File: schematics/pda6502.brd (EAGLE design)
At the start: 100 x 80 mm, 35 parts, among them IC1 74HC00D, IC2 74HC138D, IC3 DS1813-SMD, J1 CON_HEADER_2X07-PTH, U1 W65C02S, U2 W65C22S, U3 28C256, U4 UM61256AK-12

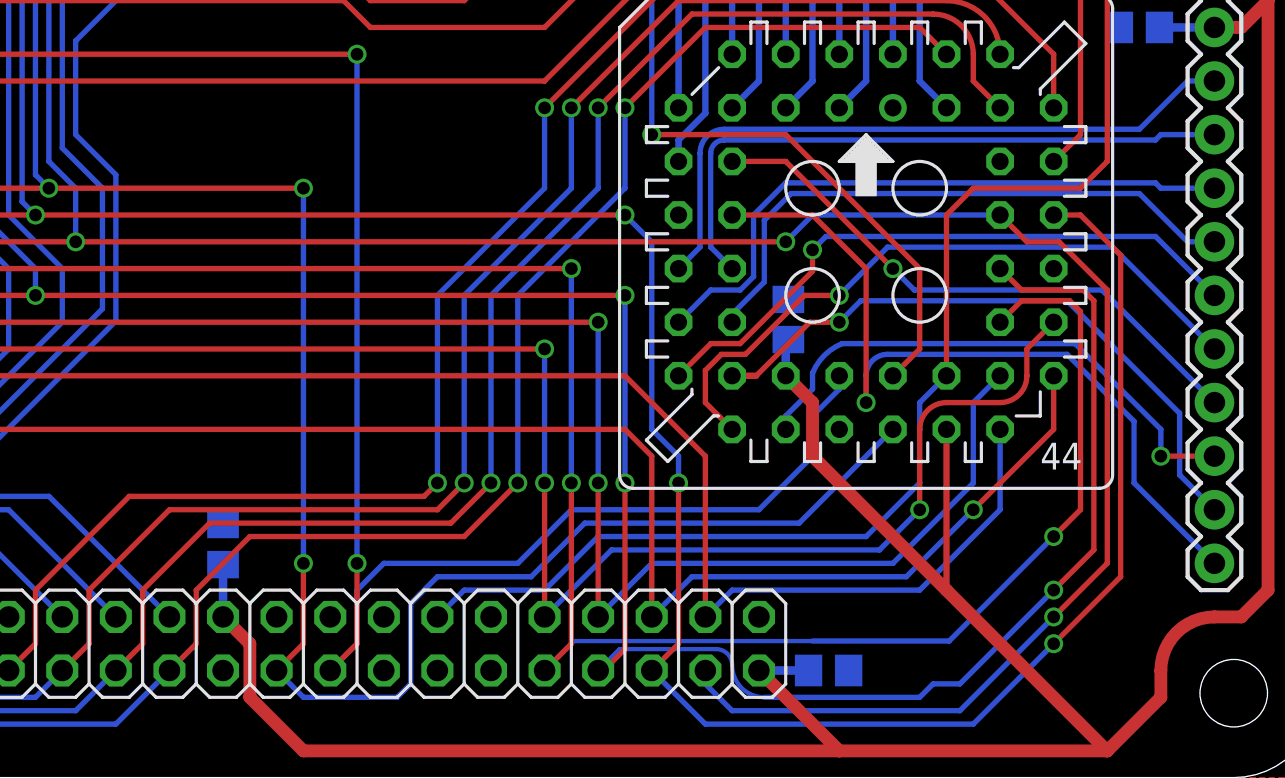
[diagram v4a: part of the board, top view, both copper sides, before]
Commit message: board: tweaks to maximize bottom GND plane; 4 airwires.
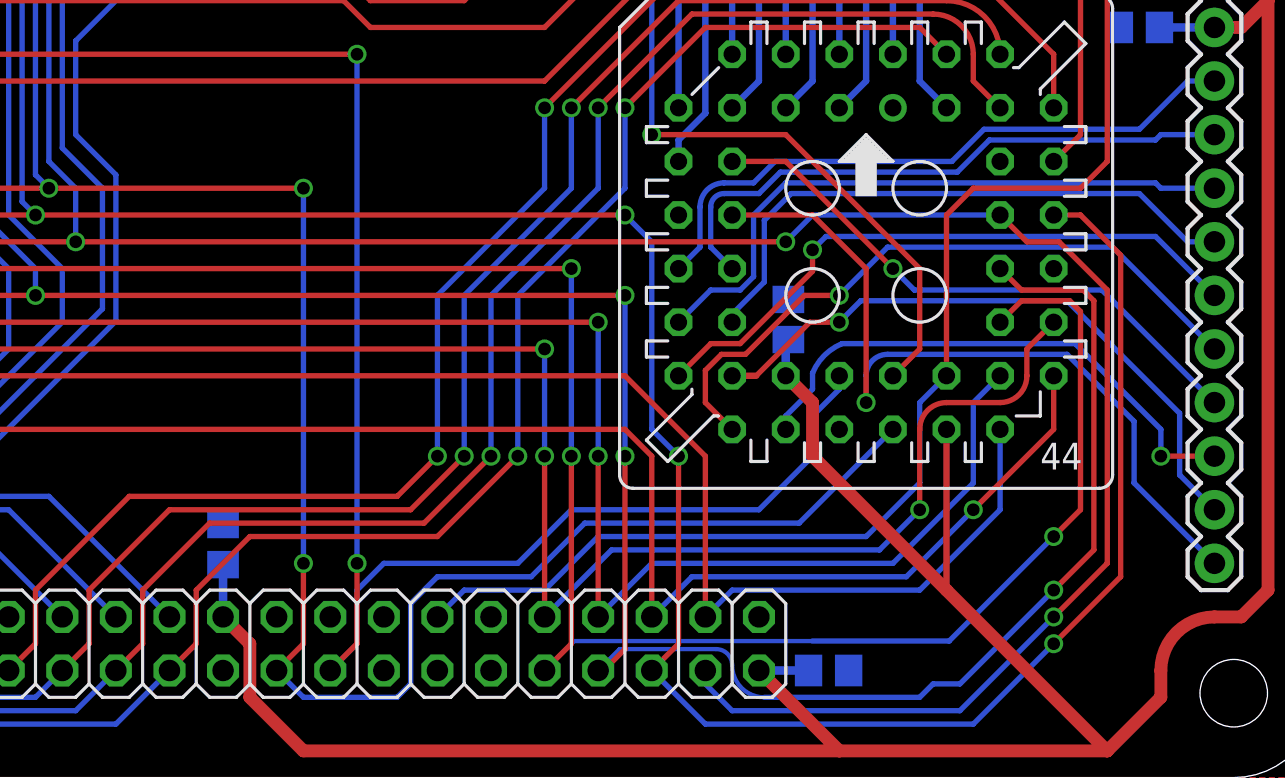
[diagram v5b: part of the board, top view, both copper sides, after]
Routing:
- net PB3: track 30.1 -> 28.6 mm
- net PB2: track 31.7 -> 30.2 mm
- net ADDR2: track 203.2 -> 202.4 mm
- net ADDR1: track 200.4 -> 199.6 mm
- net ADDR3: track 218.4 -> 217.6 mm
- net ADDR0: track 198.0 -> 197.3 mm
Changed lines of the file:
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@@
 <wire x1="35.56" y1="21.59" x2="66.04" y2="21.59" width="0.254" layer="1"/>
 <via x="66.04" y="21.59" extent="1-16" drill="0.6"/>
-<wire x1="66.04" y1="21.59" x2="66.04" y2="13.97" width="0.254" layer="16"/>
-<via x="66.04" y="13.97" extent="1-16" drill="0.6"/>
-<wire x1="66.04" y1="13.97" x2="66.04" y2="7.62" width="0.254" layer="1"/>
+<wire x1="66.04" y1="21.59" x2="66.04" y2="15.24" width="0.254" layer="16"/>
+<via x="66.04" y="15.24" extent="1-16" drill="0.6"/>
+<wire x1="66.04" y1="15.24" x2="66.04" y2="7.62" width="0.254" layer="1"/>
 </signal>
 <signal name="DATA4">
@@
 <wire x1="36.83" y1="20.32" x2="63.5" y2="20.32" width="0.254" layer="1"/>
 <via x="63.5" y="20.32" extent="1-16" drill="0.6"/>
-<wire x1="63.5" y1="20.32" x2="63.5" y2="13.97" width="0.254" layer="16"/>
-<via x="63.5" y="13.97" extent="1-16" drill="0.6"/>
-<wire x1="63.5" y1="13.97" x2="63.5" y2="7.62" width="0.254" layer="1"/>
+<wire x1="63.5" y1="20.32" x2="63.5" y2="15.24" width="0.254" layer="16"/>
+<via x="63.5" y="15.24" extent="1-16" drill="0.6"/>
+<wire x1="63.5" y1="15.24" x2="63.5" y2="7.62" width="0.254" layer="1"/>
 </signal>
 <signal name="DATA3">
@@
 <wire x1="36.83" y1="24.13" x2="64.77" y2="24.13" width="0.254" layer="1"/>
 <via x="64.77" y="24.13" extent="1-16" drill="0.6"/>
-<wire x1="64.77" y1="24.13" x2="64.77" y2="13.97" width="0.254" layer="16"/>
-<via x="64.77" y="13.97" extent="1-16" drill="0.6"/>
-<wire x1="64.77" y1="13.97" x2="64.77" y2="6.35" width="0.254" layer="1"/>
+<wire x1="64.77" y1="24.13" x2="64.77" y2="15.24" width="0.254" layer="16"/>
+<via x="64.77" y="15.24" extent="1-16" drill="0.6"/>
+<wire x1="64.77" y1="15.24" x2="64.77" y2="6.35" width="0.254" layer="1"/>
 <wire x1="64.77" y1="6.35" x2="63.5" y2="5.08" width="0.254" layer="1"/>
 </signal>
@@
 <wire x1="72.39" y1="5.334" x2="73.914" y2="3.81" width="0.2032" layer="16" curve="90"/>
 <via x="67.31" y="22.86" extent="1-16" drill="0.6"/>
-<wire x1="67.31" y1="22.86" x2="67.31" y2="13.97" width="0.254" layer="16"/>
-<via x="67.31" y="13.97" extent="1-16" drill="0.6"/>
-<wire x1="67.31" y1="13.97" x2="67.31" y2="6.096" width="0.254" layer="1"/>
+<wire x1="67.31" y1="22.86" x2="67.31" y2="15.24" width="0.254" layer="16"/>
+<via x="67.31" y="15.24" extent="1-16" drill="0.6"/>
+<wire x1="67.31" y1="15.24" x2="67.31" y2="6.096" width="0.254" layer="1"/>
 <wire x1="67.31" y1="6.096" x2="66.294" y2="5.08" width="0.254" layer="1"/>
 <wire x1="66.294" y1="5.08" x2="66.04" y2="5.08" width="0.254" layer="1"/>
@@
 <wire x1="68.58" y1="25.4" x2="68.58" y2="16.51" width="0.254" layer="16"/>
 <wire x1="68.58" y1="16.51" x2="69.85" y2="15.24" width="0.254" layer="16"/>
-<wire x1="69.85" y1="15.24" x2="69.85" y2="13.97" width="0.254" layer="16"/>
-<via x="69.85" y="13.97" extent="1-16" drill="0.6"/>
-<wire x1="69.85" y1="13.97" x2="69.85" y2="6.35" width="0.254" layer="1"/>
+<via x="69.85" y="15.24" extent="1-16" drill="0.6"/>
+<wire x1="69.85" y1="15.24" x2="69.85" y2="6.35" width="0.254" layer="1"/>
 <wire x1="69.85" y1="6.35" x2="68.58" y2="5.08" width="0.254" layer="1"/>
 </signal>
@@
 <wire x1="46.99" y1="6.35" x2="46.99" y2="8.89" width="0.254" layer="1"/>
 <wire x1="46.99" y1="8.89" x2="49.53" y2="11.43" width="0.254" layer="1"/>
-<wire x1="49.53" y1="11.43" x2="59.69" y2="11.43" width="0.254" layer="1"/>
-<wire x1="59.69" y1="11.43" x2="62.23" y2="13.97" width="0.254" layer="1"/>
-<via x="62.23" y="13.97" extent="1-16" drill="0.6"/>
-<wire x1="62.23" y1="13.97" x2="62.23" y2="22.86" width="0.254" layer="16"/>
+<wire x1="49.53" y1="11.43" x2="58.42" y2="11.43" width="0.254" layer="1"/>
+<wire x1="58.42" y1="11.43" x2="62.23" y2="15.24" width="0.254" layer="1"/>
+<via x="62.23" y="15.24" extent="1-16" drill="0.6"/>
+<wire x1="62.23" y1="15.24" x2="62.23" y2="22.86" width="0.254" layer="16"/>
 <wire x1="62.23" y1="22.86" x2="67.31" y2="27.94" width="0.254" layer="16"/>
 <wire x1="67.31" y1="27.94" x2="67.31" y2="31.75" width="0.254" layer="16"/>
@@
 <wire x1="44.45" y1="6.35" x2="44.45" y2="8.89" width="0.254" layer="1"/>
 <wire x1="44.45" y1="8.89" x2="47.625" y2="12.065" width="0.254" layer="1"/>
-<wire x1="47.625" y1="12.065" x2="59.055" y2="12.065" width="0.254" layer="1"/>
-<wire x1="59.055" y1="12.065" x2="60.96" y2="13.97" width="0.254" layer="1"/>
-<via x="60.96" y="13.97" extent="1-16" drill="0.6"/>
-<wire x1="60.96" y1="13.97" x2="60.96" y2="22.86" width="0.254" layer="16"/>
+<wire x1="47.625" y1="12.065" x2="57.785" y2="12.065" width="0.254" layer="1"/>
+<wire x1="57.785" y1="12.065" x2="60.96" y2="15.24" width="0.254" layer="1"/>
+<via x="60.96" y="15.24" extent="1-16" drill="0.6"/>
+<wire x1="60.96" y1="15.24" x2="60.96" y2="22.86" width="0.254" layer="16"/>
 <wire x1="60.96" y1="22.86" x2="66.04" y2="27.94" width="0.254" layer="16"/>
 <wire x1="66.04" y1="27.94" x2="66.04" y2="31.75" width="0.254" layer="16"/>
@@
 <wire x1="41.91" y1="6.35" x2="41.91" y2="8.89" width="0.254" layer="1"/>
 <wire x1="41.91" y1="8.89" x2="45.72" y2="12.7" width="0.254" layer="1"/>
-<wire x1="45.72" y1="12.7" x2="58.42" y2="12.7" width="0.254" layer="1"/>
-<wire x1="58.42" y1="12.7" x2="59.69" y2="13.97" width="0.254" layer="1"/>
-<via x="59.69" y="13.97" extent="1-16" drill="0.6"/>
-<wire x1="59.69" y1="13.97" x2="59.69" y2="22.86" width="0.254" layer="16"/>
+<wire x1="45.72" y1="12.7" x2="57.15" y2="12.7" width="0.254" layer="1"/>
+<wire x1="57.15" y1="12.7" x2="59.69" y2="15.24" width="0.254" layer="1"/>
+<via x="59.69" y="15.24" extent="1-16" drill="0.6"/>
+<wire x1="59.69" y1="15.24" x2="59.69" y2="22.86" width="0.254" layer="16"/>
 <wire x1="59.69" y1="22.86" x2="64.77" y2="27.94" width="0.254" layer="16"/>
 <wire x1="64.77" y1="27.94" x2="64.77" y2="31.75" width="0.254" layer="16"/>
@@
 <wire x1="39.37" y1="6.35" x2="39.37" y2="8.89" width="0.254" layer="1"/>
 <wire x1="39.37" y1="8.89" x2="43.815" y2="13.335" width="0.254" layer="1"/>
-<wire x1="43.815" y1="13.335" x2="57.785" y2="13.335" width="0.254" layer="1"/>
-<wire x1="57.785" y1="13.335" x2="58.42" y2="13.97" width="0.254" layer="1"/>
-<via x="58.42" y="13.97" extent="1-16" drill="0.6"/>
-<wire x1="58.42" y1="13.97" x2="58.42" y2="22.86" width="0.254" layer="16"/>
+<wire x1="43.815" y1="13.335" x2="56.515" y2="13.335" width="0.254" layer="1"/>
+<wire x1="56.515" y1="13.335" x2="58.42" y2="15.24" width="0.254" layer="1"/>
+<via x="58.42" y="15.24" extent="1-16" drill="0.6"/>
+<wire x1="58.42" y1="15.24" x2="58.42" y2="22.86" width="0.254" layer="16"/>
 <wire x1="58.42" y1="22.86" x2="63.5" y2="27.94" width="0.254" layer="16"/>
 <wire x1="63.5" y1="27.94" x2="63.5" y2="31.75" width="0.254" layer="16"/>
@@
 <wire x1="52.705" y1="54.295" x2="58.42" y2="50.2666" width="0" layer="19" extent="1-1"/>
 <wire x1="97.57" y1="69.85" x2="95.25" y2="60.96" width="0" layer="19" extent="1-1"/>
-<wire x1="80.01" y1="31.75" x2="90.744" y2="35.56" width="0" layer="19" extent="16-16"/>
-<wire x1="75.057" y1="22.667" x2="80.01" y2="31.75" width="0" layer="19" extent="16-16"/>
 </signal>
 <signal name="5V">
@@
 <wire x1="95.25" y1="33.02" x2="93.98" y2="33.02" width="0.254" layer="16"/>
 <wire x1="93.98" y1="33.02" x2="91.694" y2="30.734" width="0.254" layer="16"/>
-<wire x1="91.694" y1="30.734" x2="72.009" y2="30.734" width="0.254" layer="16"/>
-<wire x1="72.009" y1="30.734" x2="70.866" y2="29.591" width="0.254" layer="16" curve="90"/>
-<wire x1="70.866" y1="29.591" x2="70.866" y2="25.146" width="0.254" layer="16"/>
+<wire x1="72.009" y1="28.194" x2="70.866" y2="27.051" width="0.254" layer="16" curve="90"/>
+<wire x1="70.866" y1="27.051" x2="70.866" y2="25.146" width="0.254" layer="16"/>
 <wire x1="70.866" y1="25.146" x2="69.85" y2="24.13" width="0.254" layer="16"/>
+<wire x1="72.009" y1="28.194" x2="73.406" y2="28.194" width="0.254" layer="16"/>
+<wire x1="73.406" y1="28.194" x2="74.422" y2="29.21" width="0.254" layer="16"/>
+<wire x1="74.422" y1="29.21" x2="82.804" y2="29.21" width="0.254" layer="16"/>
+<wire x1="82.804" y1="29.21" x2="84.328" y2="30.734" width="0.254" layer="16"/>
+<wire x1="84.328" y1="30.734" x2="91.694" y2="30.734" width="0.254" layer="16"/>
 </signal>
 <signal name="PB3">
 <contactref element="U2" pad="14"/>
 <contactref element="JP4" pad="4"/>
-<wire x1="92.456" y1="30.226" x2="72.009" y2="30.226" width="0.254" layer="16"/>
-<wire x1="72.009" y1="30.226" x2="71.374" y2="29.591" width="0.254" layer="16" curve="90"/>
-<wire x1="71.374" y1="29.591" x2="71.374" y2="25.146" width="0.254" layer="16"/>
+<wire x1="72.009" y1="27.686" x2="71.374" y2="27.051" width="0.254" layer="16" curve="90"/>
+<wire x1="71.374" y1="27.051" x2="71.374" y2="25.146" width="0.254" layer="16"/>
 <wire x1="71.374" y1="25.146" x2="72.39" y2="24.13" width="0.254" layer="16"/>
 <wire x1="95.25" y1="30.48" x2="92.71" y2="30.48" width="0.254" layer="16"/>
 <wire x1="92.71" y1="30.48" x2="92.456" y2="30.226" width="0.254" layer="16"/>
+<wire x1="72.009" y1="27.686" x2="73.66" y2="27.686" width="0.254" layer="16"/>
+<wire x1="73.66" y1="27.686" x2="74.676" y2="28.702" width="0.254" layer="16"/>
+<wire x1="74.676" y1="28.702" x2="83.058" y2="28.702" width="0.254" layer="16"/>
+<wire x1="83.058" y1="28.702" x2="84.582" y2="30.226" width="0.254" layer="16"/>
+<wire x1="84.582" y1="30.226" x2="92.456" y2="30.226" width="0.254" layer="16"/>
 </signal>
 <signal name="PB4">

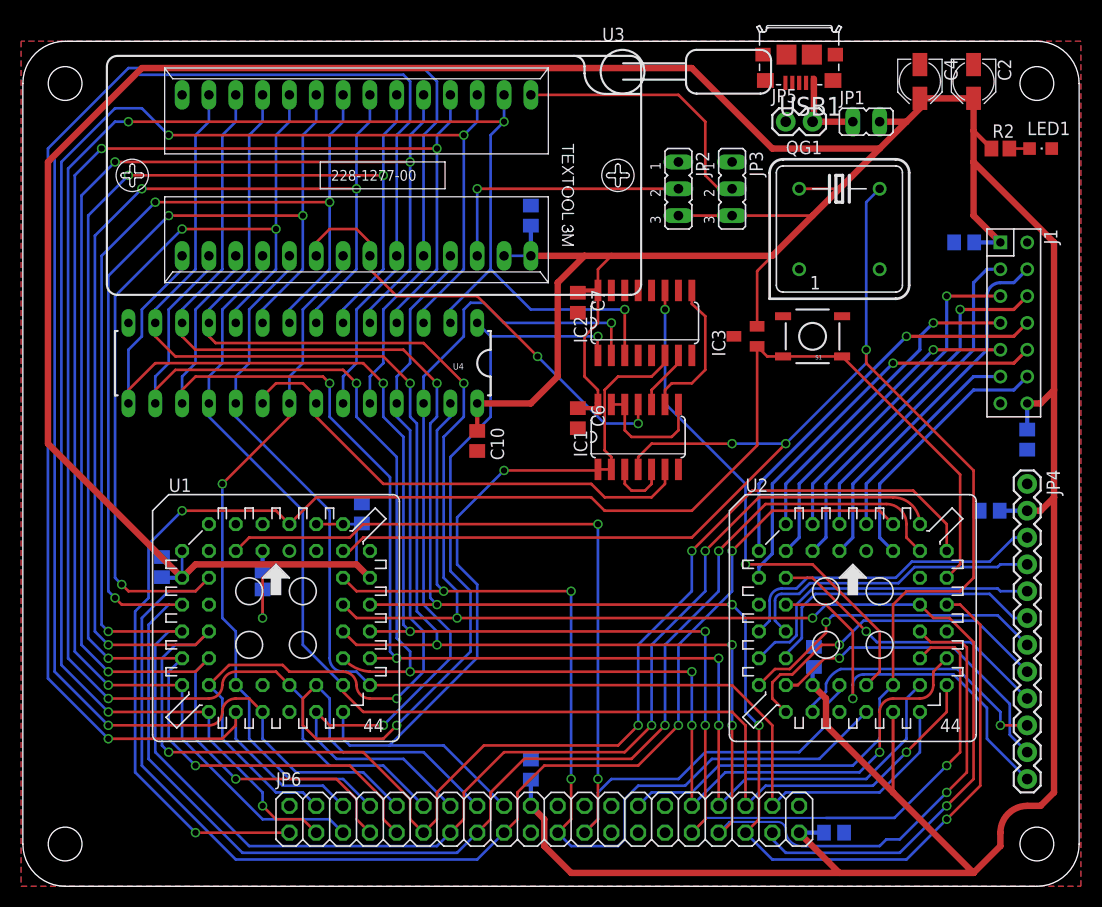
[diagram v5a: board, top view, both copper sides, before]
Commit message: board: vias under RAM adjusted; 3 airwires remaining.
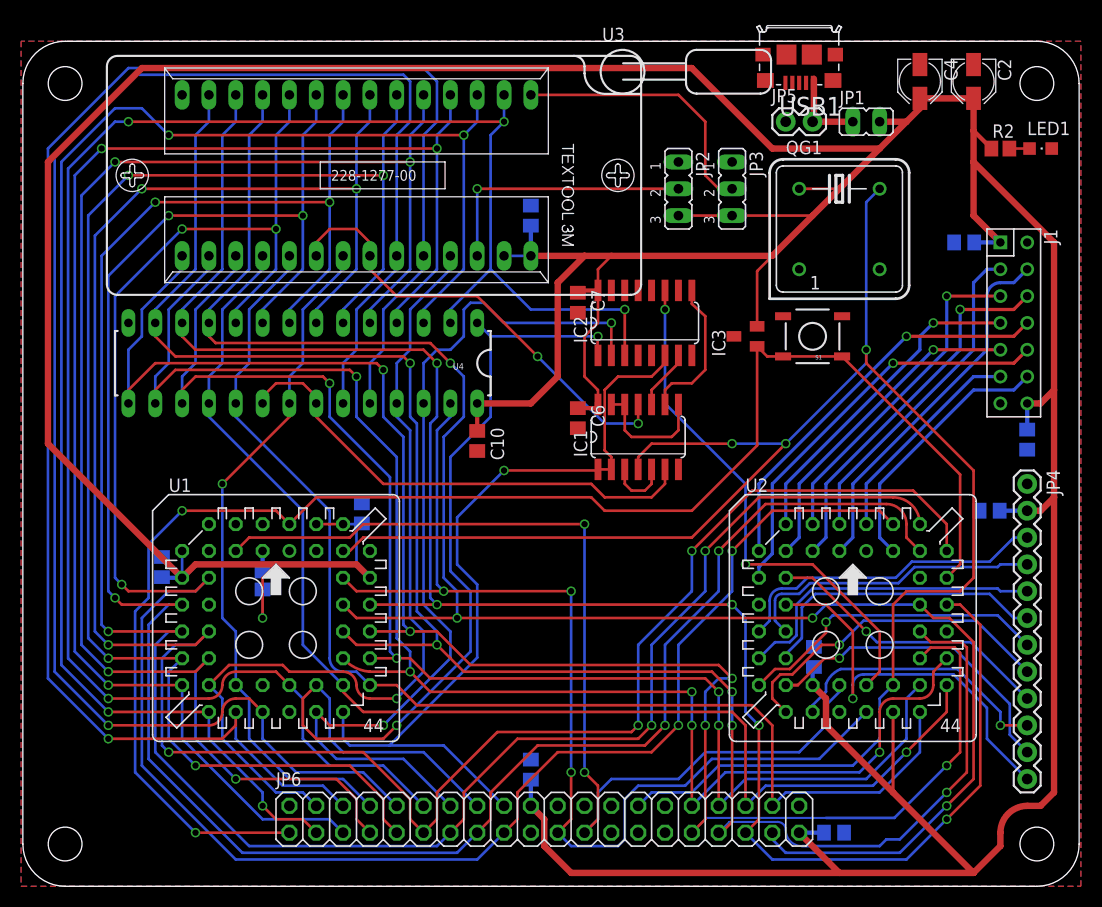
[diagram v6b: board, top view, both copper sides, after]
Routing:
- net DATA3: track 161.6 -> 164.1 mm
- net DATA5: track 133.8 -> 131.9 mm
- net DATA2: track 177.2 -> 175.7 mm
- net DATA1: track 175.2 -> 176.4 mm
- net DATA4: track 146.0 -> 145.3 mm
- net IRQB: track 98.0 -> 97.2 mm
- net ADDR13: track 87.5 -> 88.2 mm
